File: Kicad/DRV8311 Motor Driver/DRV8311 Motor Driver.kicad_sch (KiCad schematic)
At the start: 19 parts, among them J1 1.27mm pin header, J2 1.27mm pin header, J4 Molex Picoblade, U1 DRV8311HRRWR

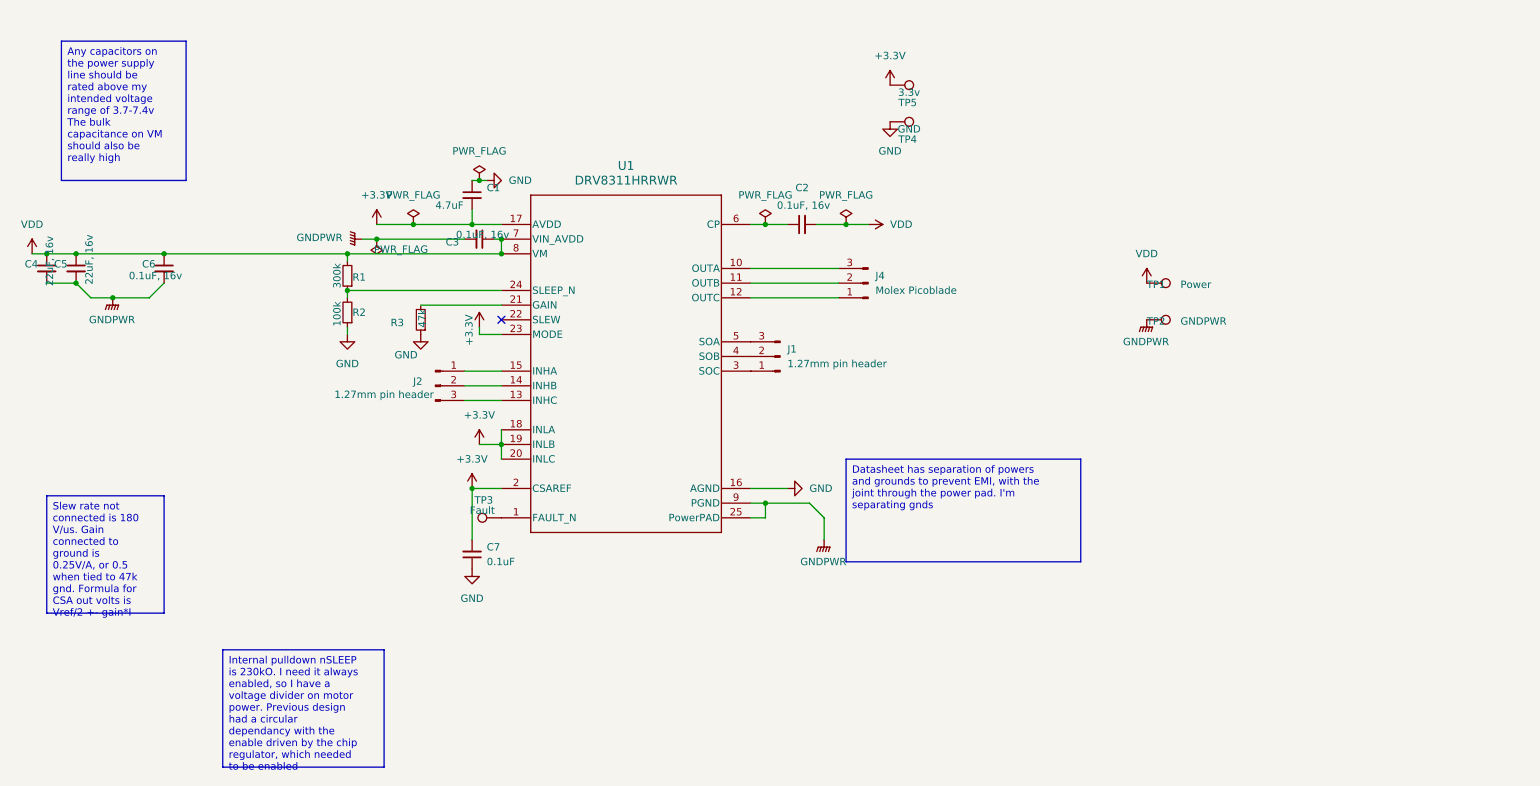
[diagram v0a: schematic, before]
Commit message: Replaced external connectors
I have keystone smd low profile contacts for the power, and 1.27mm pitch headers for the data pins.
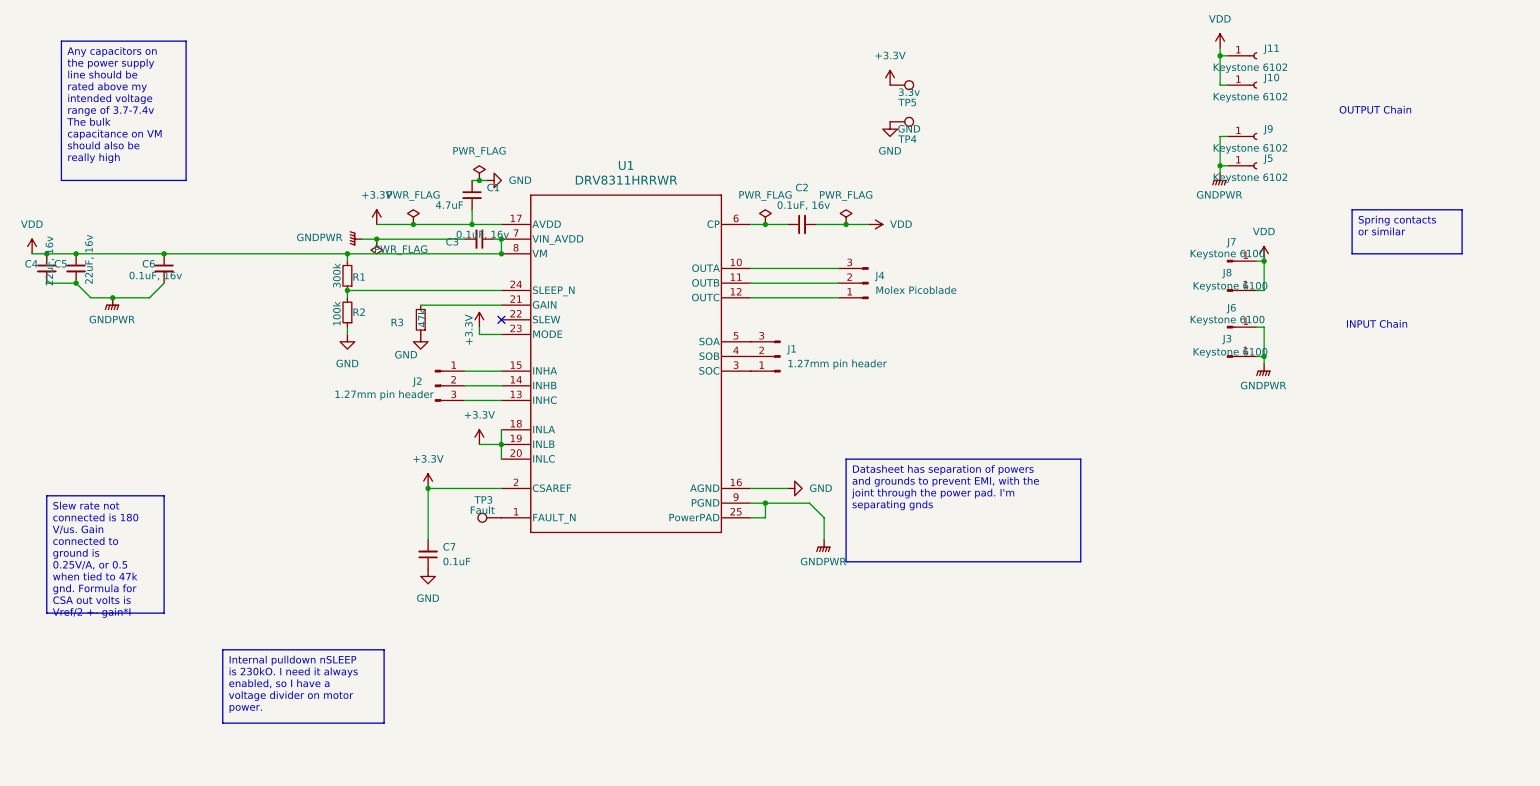
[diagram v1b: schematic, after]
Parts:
- removed TP1: Power, TestPoint:TestPoint_Pad_D2.0mm, symbol Connector:TestPoint
- removed TP2: GNDPWR, TestPoint:TestPoint_Pad_D2.0mm, symbol Connector:TestPoint
- added J10, J11, J5, J9: Keystone 6102, 6102:KEYSTONE_6102, symbol Connector:Conn_01x01_Socket
- added J3, J6, J7, J8: Keystone 6100, 6100:KEYSTONE_6100, symbol Connector:Conn_01x01_Pin
- J1, J2: footprint (none) -> Connector_PinHeader_1.27mm:PinHeader_1x03_P1.27mm_Horizontal
- J4: footprint (none) -> Connector_Molex:Molex_PicoBlade_53048-0310_1x03_P1.25mm_Horizontal
- TP3, TP4, TP5: footprint (none) -> TestPoint:TestPoint_Pad_D1.0mm
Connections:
- net GNDPWR: now also J3.1 (Pin_1), J5.1 (Pin_1), J6.1 (Pin_1), J9.1 (Pin_1)
- net VDD: now also J10.1 (Pin_1), J11.1 (Pin_1), J7.1 (Pin_1), J8.1 (Pin_1)
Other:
- note added: "INPUT Chain"
- note added: "OUTPUT Chain"
- moved on the sheet: C7

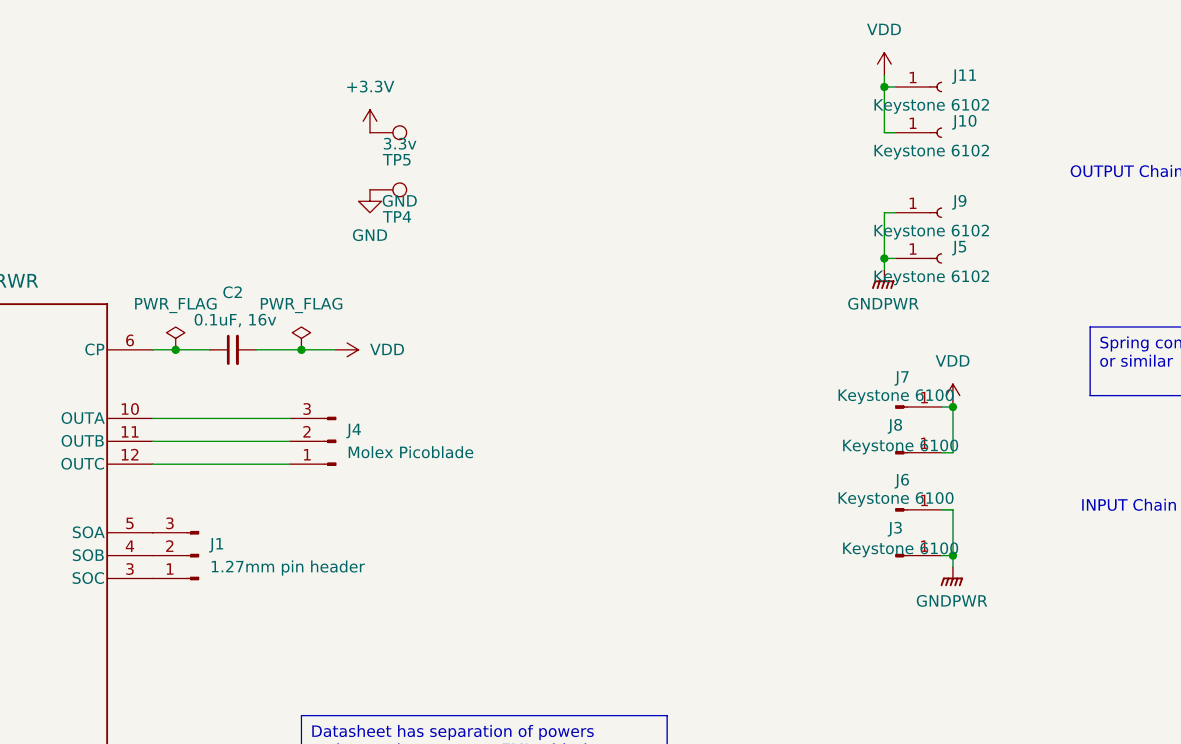
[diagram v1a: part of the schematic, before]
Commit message: Finished basic layout for motor driver card
The power connectors as of now have no way of contacting adjacent cards. The layout will need some tuning, but I think the components for the most part can stay in the same place.
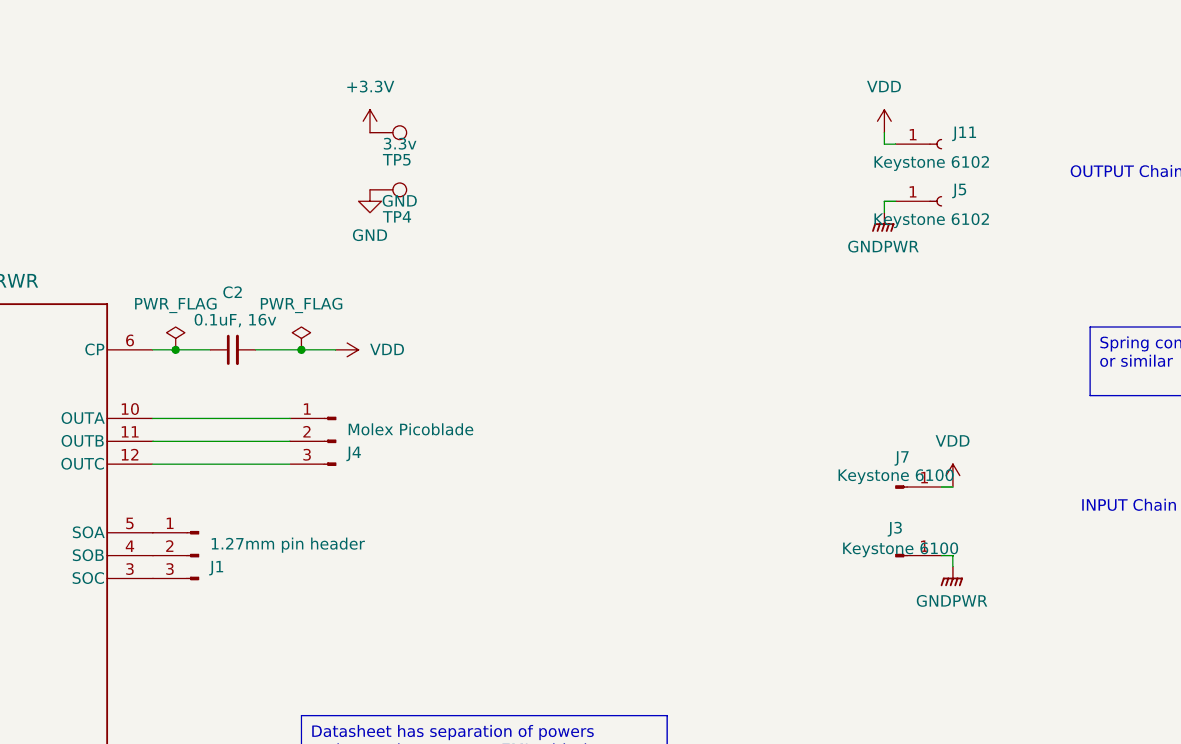
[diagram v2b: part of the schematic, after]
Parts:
- removed J10, J9: Keystone 6102, 6102:KEYSTONE_6102, symbol Connector:Conn_01x01_Socket
- removed J6, J8: Keystone 6100, 6100:KEYSTONE_6100, symbol Connector:Conn_01x01_Pin
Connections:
- net at J4.1 (Pin_1): now also U1.10 (OUTA); no longer U1.12 (OUTC)
- net at J4.3 (Pin_3): now also U1.12 (OUTC); no longer U1.10 (OUTA)
- net at J1.1 (Pin_1): now also U1.5 (SOA); no longer U1.3 (SOC)
- net at J1.3 (Pin_3): now also U1.3 (SOC); no longer U1.5 (SOA)
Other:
- moved on the sheet: J1, J11, J4, J5, J7

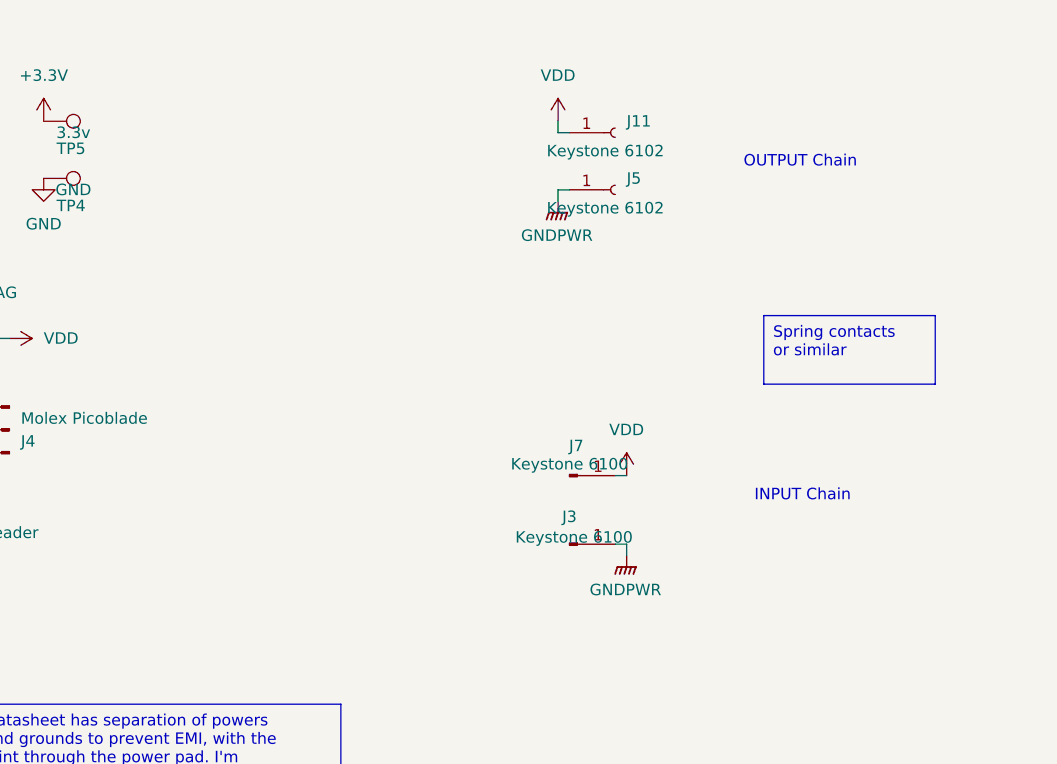
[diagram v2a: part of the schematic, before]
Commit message: Started switchout of motor power connectors
It looks like I may actually have gotten connectors a bit TOO big! I don't know if it will fit!
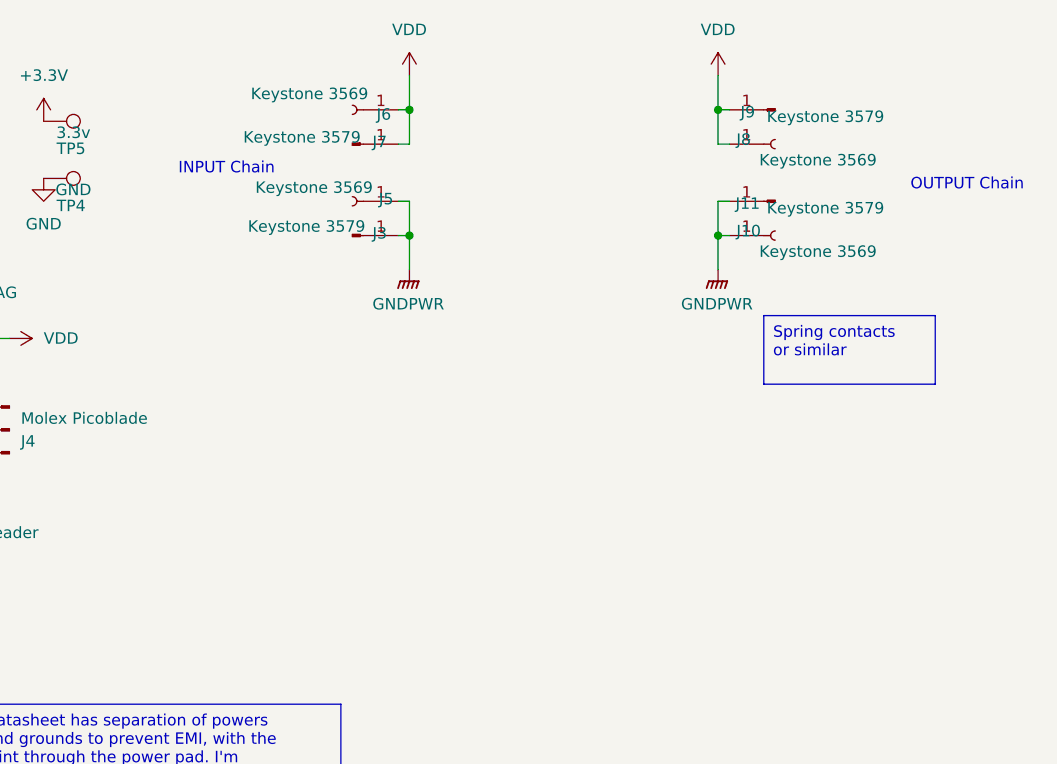
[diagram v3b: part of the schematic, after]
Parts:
- removed J11: Keystone 6102, 6102:KEYSTONE_6102, symbol Connector:Conn_01x01_Socket
- added J10, J6, J8: Keystone 3569, custom_Connector:Keystone_3569, symbol Connector:Conn_01x01_Socket
- added J11, J9: Keystone 3579, custom_Connector:Keystone_3579, symbol Connector:Conn_01x01_Pin
- J3, J7: value Keystone 6100 -> Keystone 3579; footprint 6100:KEYSTONE_6100 -> custom_Connector:Keystone_3579
- J5: value Keystone 6102 -> Keystone 3569; footprint 6102:KEYSTONE_6102 -> custom_Connector:Keystone_3569
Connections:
- net GNDPWR: now also J10.1 (Pin_1), J11.1 (Pin_1)
- net VDD: now also J6.1 (Pin_1), J8.1 (Pin_1), J9.1 (Pin_1)
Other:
- moved on the sheet: J7

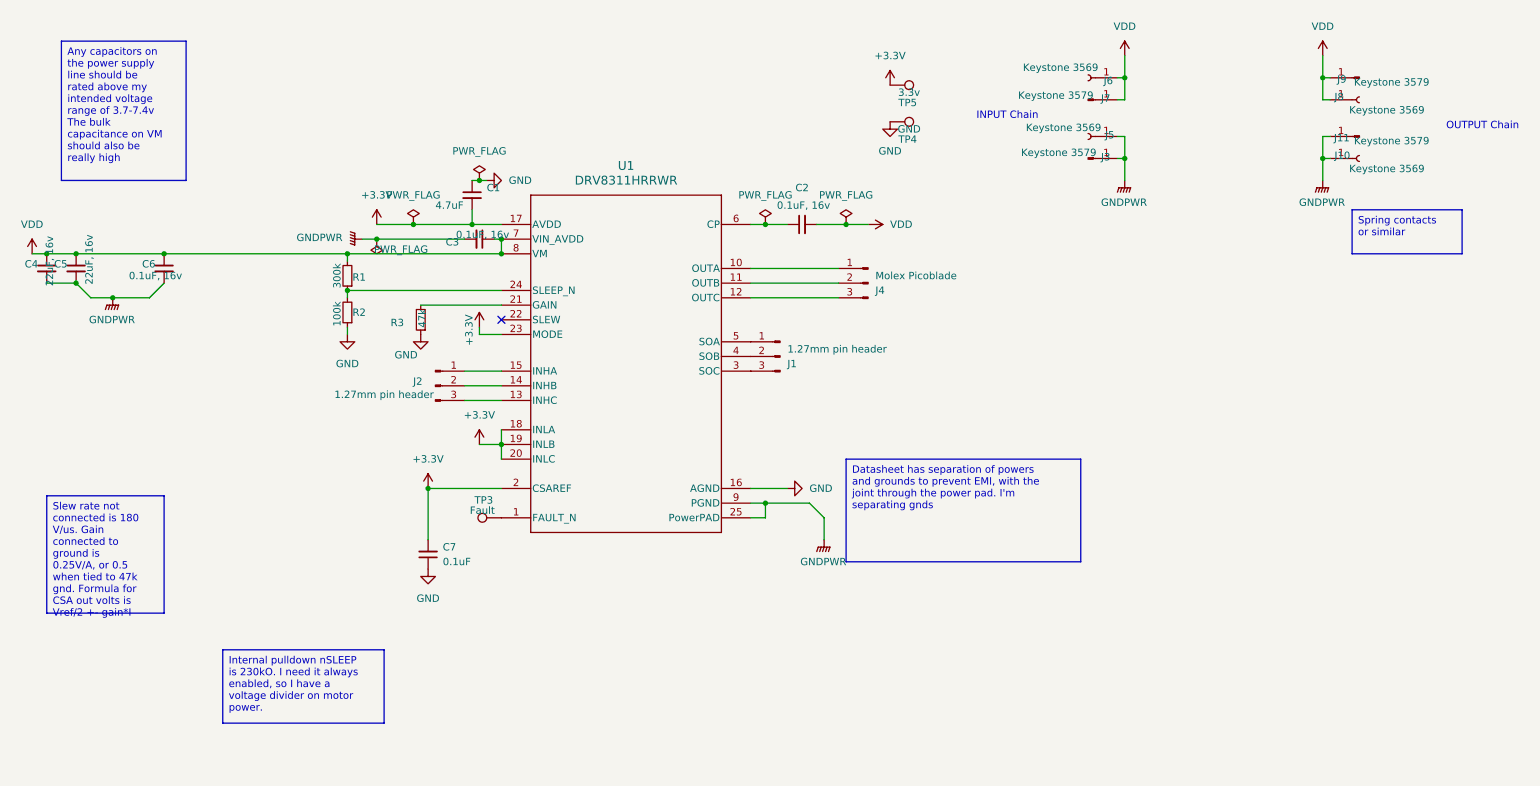
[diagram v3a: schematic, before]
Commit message: Redesigned Motor Driver module for higher current
I doubled up the connectors on the edge, and I switched to a cheaper version of the same edge connector from Keystone. I'm planning on cutting the receptor in half because the male connector does not fully use the length, and I can save space and time. This is why the footprint is sticking off the edge
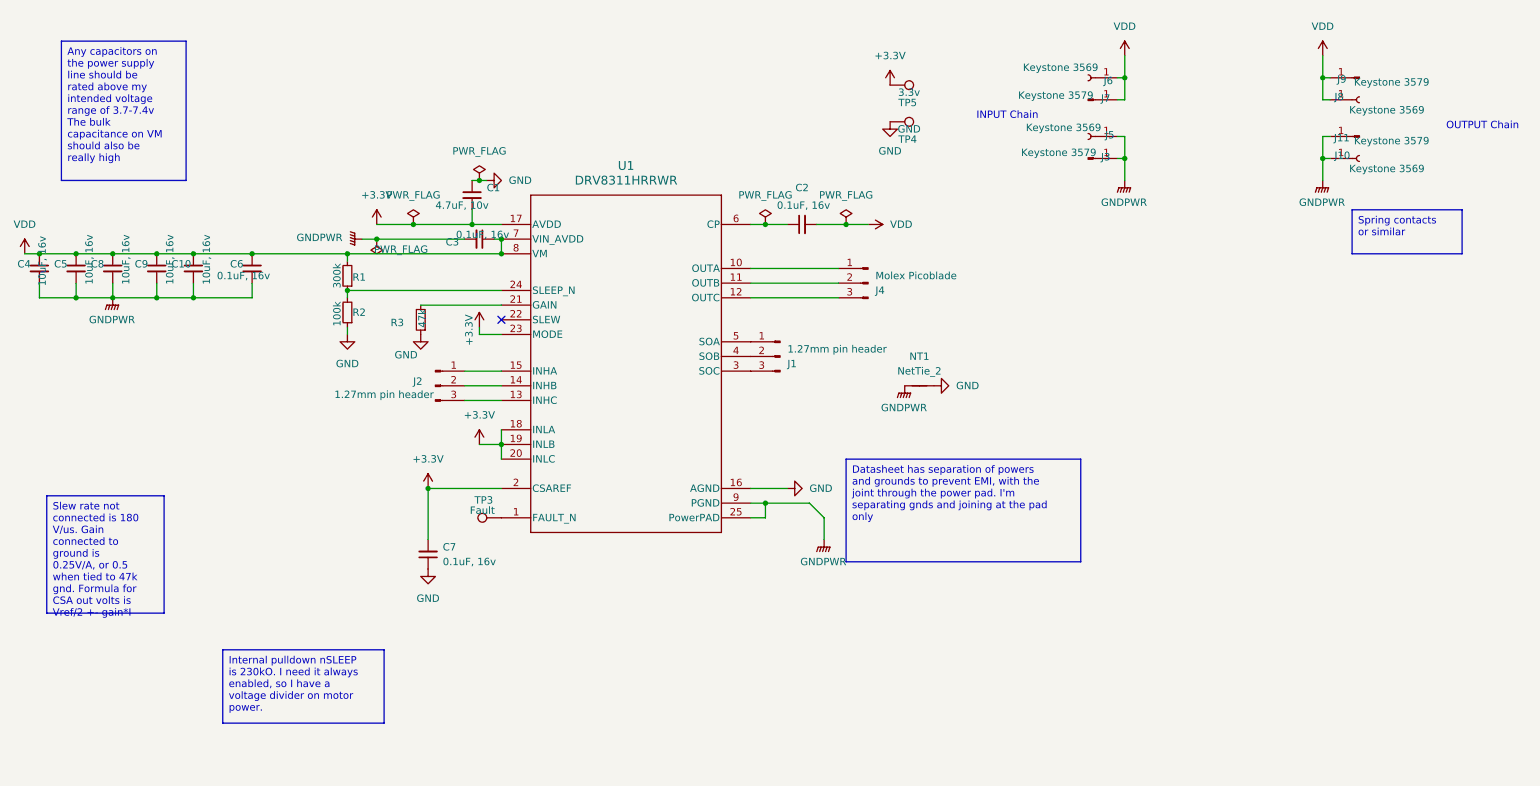
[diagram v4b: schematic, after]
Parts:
- added C10, C8, C9: 10uF, 16v, Capacitor_SMD:C_0603_1608Metric, symbol Device:C_Small
- added NT1: NetTie_2, custom_Connector:NetTie-2_SMD_Pad0.2mm, symbol Device:NetTie_2
- C1: value 4.7uF -> 4.7uF, 10v; footprint Capacitor_SMD:C_0603_1608Metric -> Capacitor_SMD:C_0402_1005Metric
- C3: footprint Capacitor_SMD:C_0603_1608Metric -> Capacitor_SMD:C_0402_1005Metric
- C4, C5: value 22uF, 16v -> 10uF, 16v
- C7: value 0.1uF -> 0.1uF, 16v; footprint Capacitor_SMD:C_0603_1608Metric -> Capacitor_SMD:C_0402_1005Metric
- R1, R2, R3: footprint Resistor_SMD:R_0603_1608Metric -> Resistor_SMD:R_0402_1005Metric
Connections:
- net GND: now also NT1.2
- net GNDPWR: now also C10.2, C8.2, C9.2, NT1.1
- net VDD: now also C10.1, C8.1, C9.1
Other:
- moved on the sheet: C4, C6
